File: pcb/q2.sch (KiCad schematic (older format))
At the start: 238 parts, among them U1 R, U10 R, U100 R, U101 R, U102 R, U103 R, U104 R, U105 R, U106 R, U107 R, U108 R, U109 R, U11 R, U110 R, U111 R, U112 R, U113 16, U114 R, U115 WiPy, U116 UDN_2981, U117 UDN_2981, U118 74HC595, U119 74HC595, U12 R, U13 R, U14 R, U15 R, U16 R, U17 R, U18 R, U19 R, U2 R, U20 R, U21 R, U22 R, U23 R, U24 R, U25 R, U26 R, U27 R, U28 R, U29 R, U3 R, U30 R, U31 R, U32 R, U33 R, U34 R, U35 R, U36 R, U37 R, U38 R, U39 R, U4 R, U40 R, U41 R, U42 R, U43 R, U44 R, U45 R, U46 R, U47 R, U48 R, U49 R, U5 R, U50 R, U51 R, U52 R, U53 R, U54 R, U55 R, U56 R, U57 R, U58 R, U59 R, U6 R, U60 R, U61 R, U62 R, U63 R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

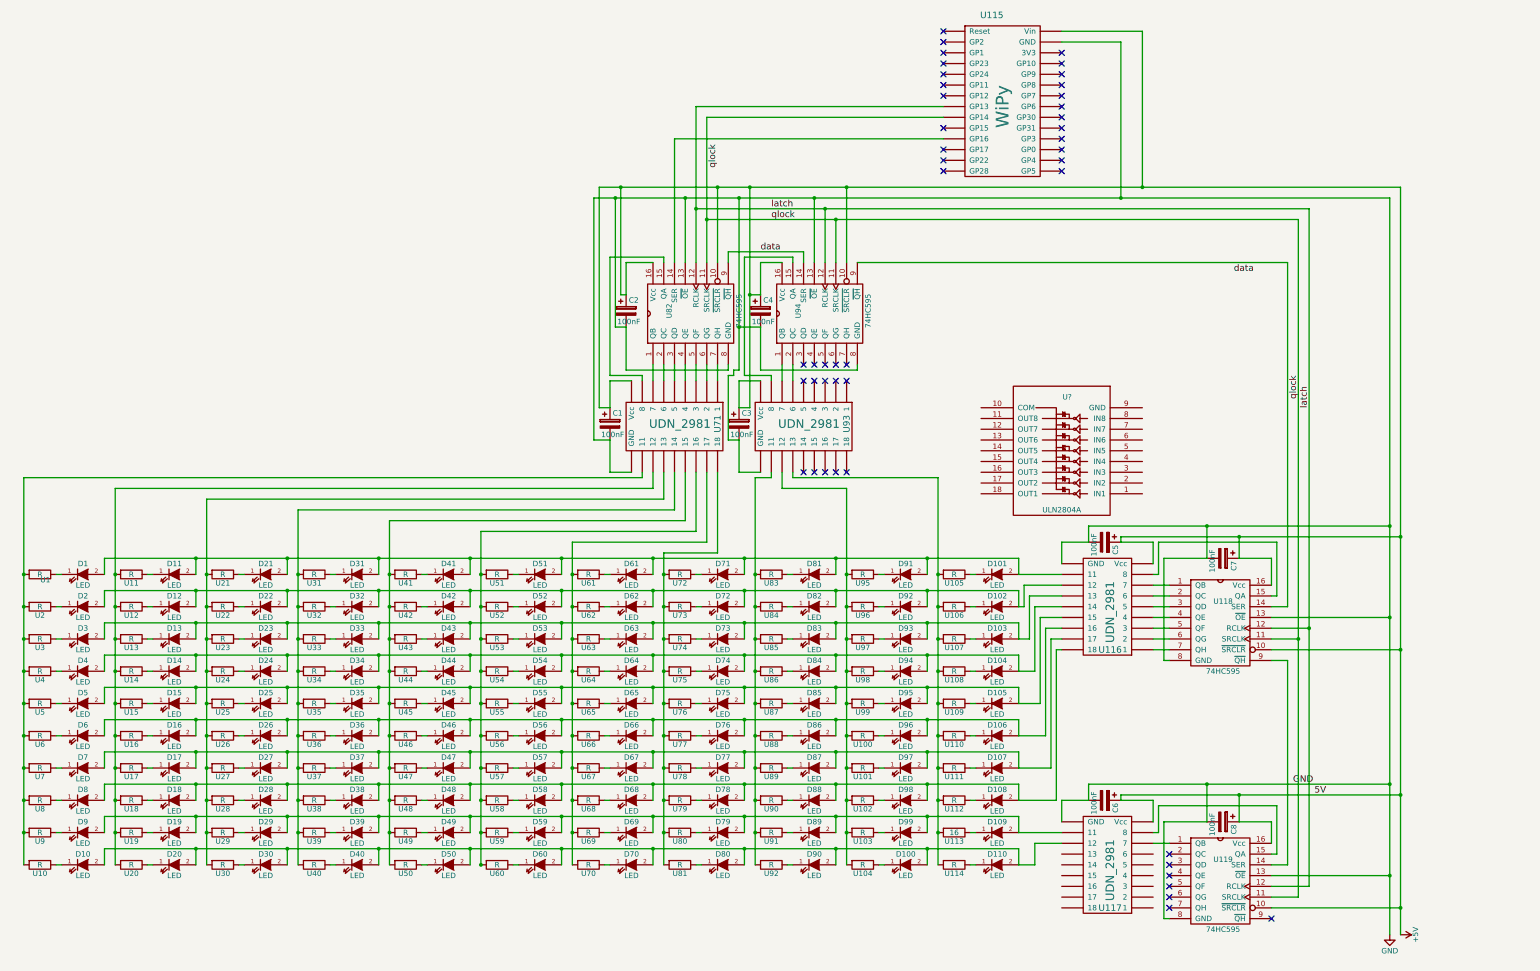
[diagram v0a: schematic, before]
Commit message: move cathode driver + SR to left side
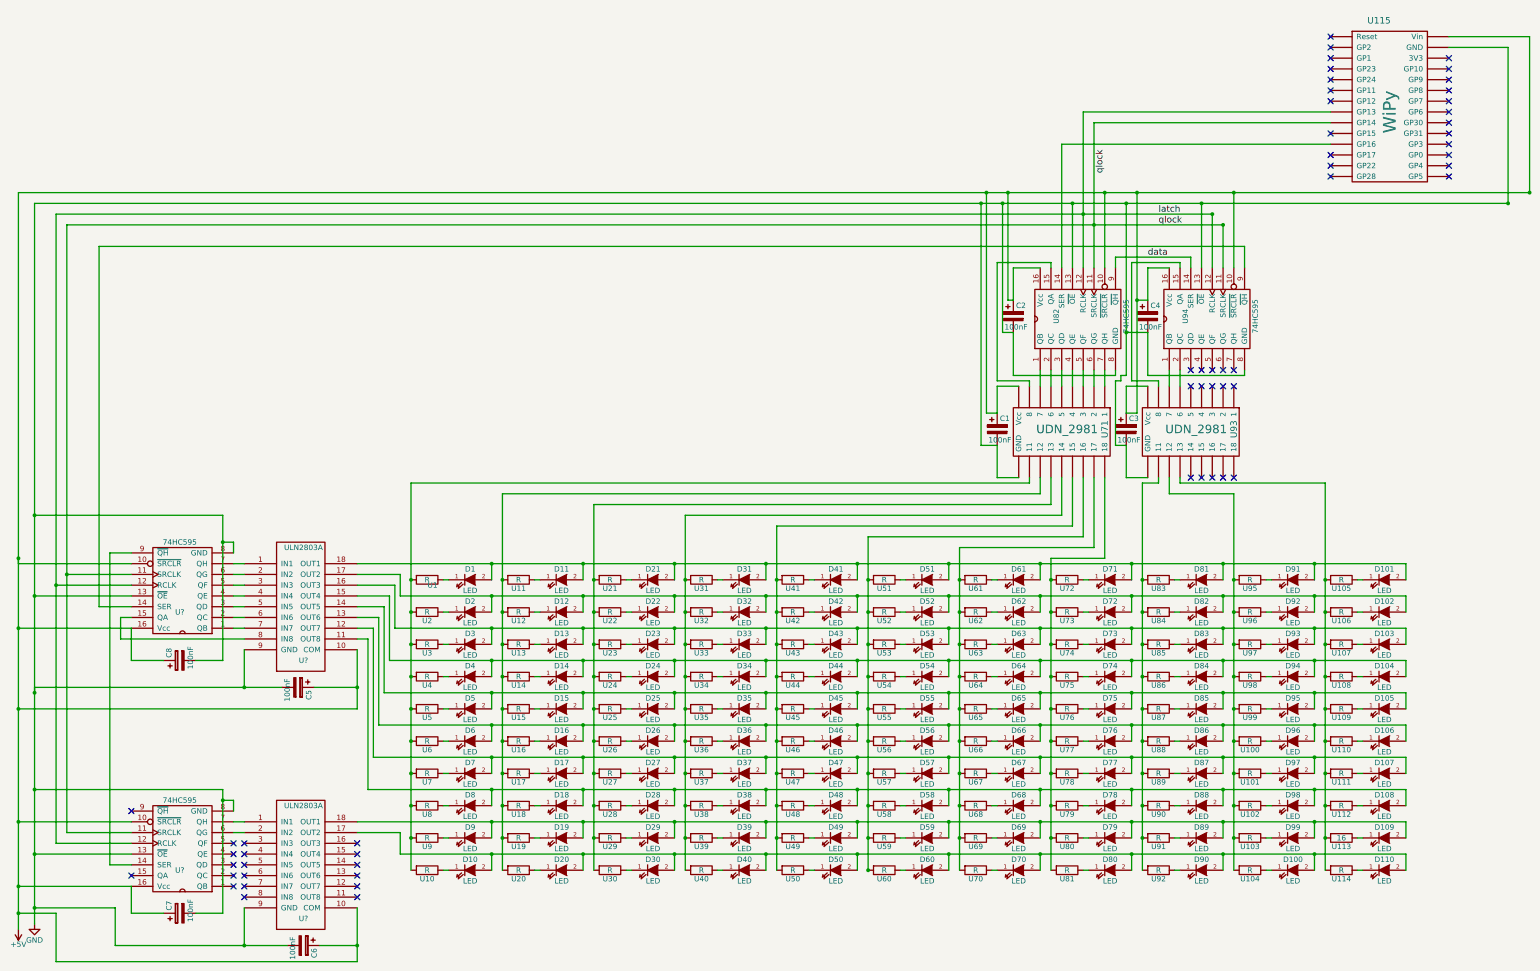
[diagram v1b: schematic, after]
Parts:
- removed U116, U117: UDN_2981, symbol UDN_2981
- removed U118, U119: 74HC595, symbol 74HC595
- removed U?: ULN2804A, symbol ULN2804A
- added U? (x2): ULN2803A, symbol ULN2803A
- added U? (x2): 74HC595, symbol 74HC595
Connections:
- net +5V: now also U?.10 (COM), U?.10 (COM), U?.10 (~SRCLR), U?.10 (~SRCLR), U?.16 (Vcc), U?.16 (Vcc)
- net GND: now also U?.13 (~OE), U?.13 (~OE), U?.8 (GND), U?.8 (GND), U?.9 (GND), U?.9 (GND)
- net latch: now also U?.12 (RCLK), U?.12 (RCLK)
- net qlock: now also U?.11 (SRCLK), U?.11 (SRCLK)
- net at D1.2 (A), D101.2 (A), D11.2 (A)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: now also U?.18 (OUT1)
- net at D102.2 (A), D12.2 (A), D2.2 (A)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: now also U?.17 (OUT2)
- net at D103.2 (A), D13.2 (A), D23.2 (A)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: now also U?.16 (OUT3)
- net at D104.2 (A), D14.2 (A), D24.2 (A)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: now also U?.15 (OUT4)
- net at D105.2 (A), D15.2 (A), D25.2 (A)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: now also U?.14 (OUT5)
- net at D106.2 (A), D16.2 (A), D26.2 (A)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: now also U?.13 (OUT6)
- net at D107.2 (A), D17.2 (A), D27.2 (A)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: now also U?.12 (OUT7)
- net at D108.2 (A), D18.2 (A), D28.2 (A)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: now also U?.11 (OUT8)
- net at D109.2 (A), D19.2 (A), D29.2 (A)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: now also U?.18 (OUT1)
- net at D10.2 (A), D100.2 (A), D110.2 (A)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: now also U?.17 (OUT2)
- net at U94.9 (~QH): now also U?.14 (SER)
- new net: U?.1 (IN1), U?.7 (QH) (x2)
- new net: U?.2 (IN2), U?.6 (QG) (x2)
- new net: U?.3 (IN3), U?.5 (QF)
- new net: U?.4 (IN4), U?.4 (QE)
- new net: U?.3 (QD), U?.5 (IN5)
- new net: U?.2 (QC), U?.6 (IN6)
- new net: U?.1 (QB), U?.7 (IN7)
- new net: U?.15 (QA), U?.8 (IN8)
- new net: U?.14 (SER), U?.9 (~QH)
- no-connect marks 45 -> 57
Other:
- moved on the sheet: C1, C2, C3, C4, C5, C6, C7, C8, D1, D10, D100, D101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

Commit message: capacitor for -OE to disable row shift register at startup
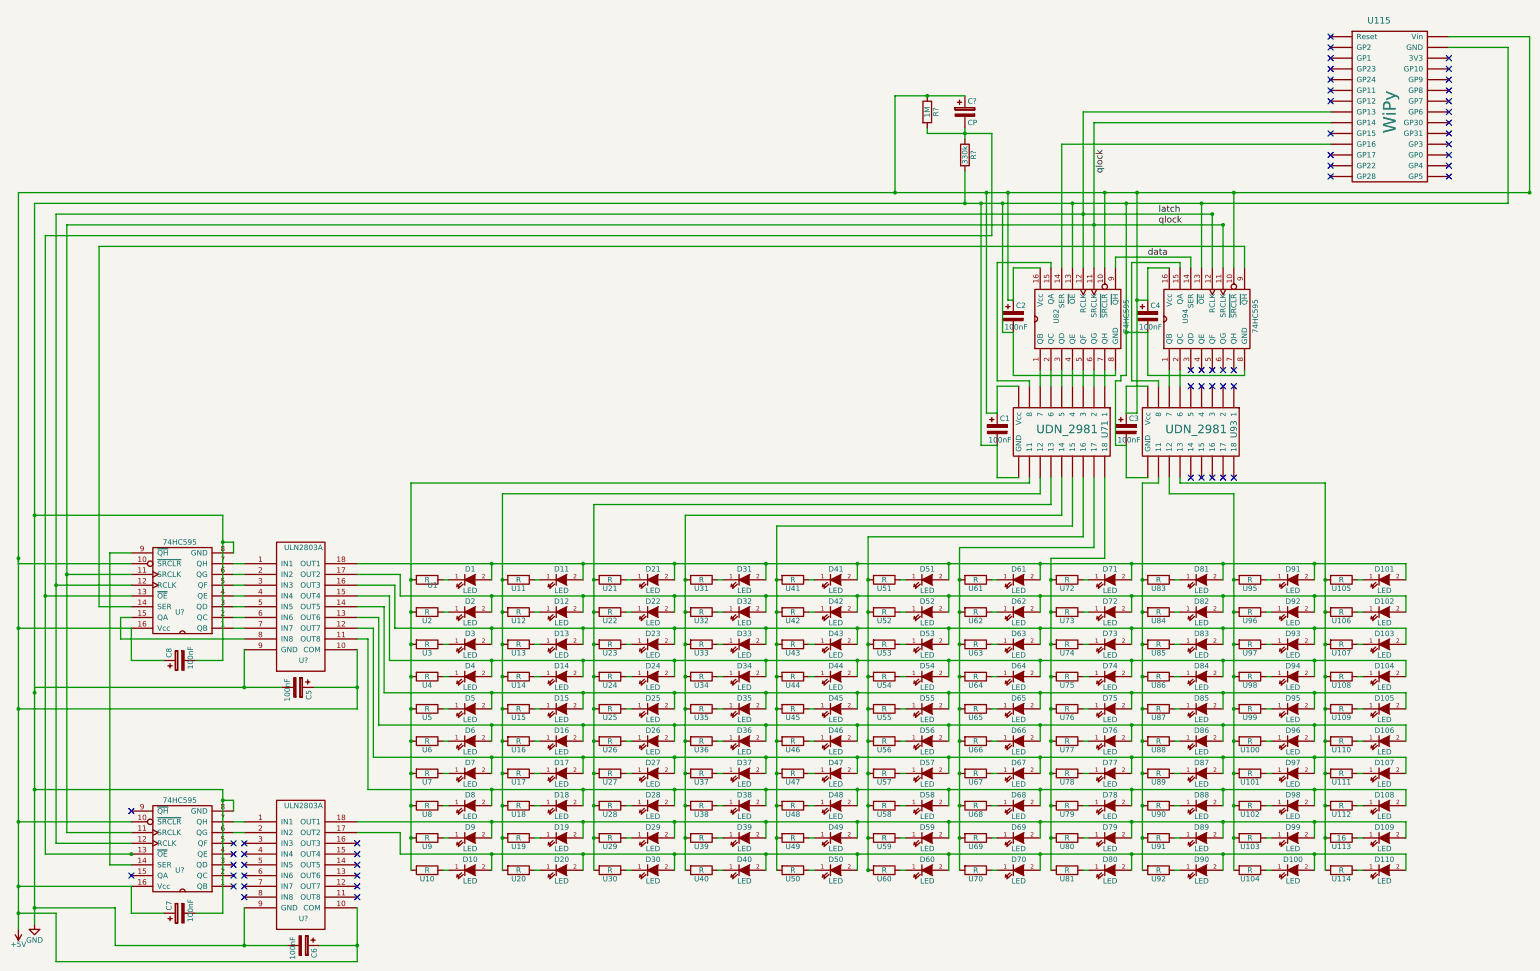
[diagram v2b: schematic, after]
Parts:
- added C?: CP, symbol CP
- added R?: 1M, symbol R
- added R?: 330k, symbol R
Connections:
- net +5V: now also C?.1, R?.1
- net GND: now also R?.2; no longer U?.13 (~OE), U?.13 (~OE)
- new net: C?.2, R?.1, R?.2, U?.13 (~OE), U?.13 (~OE)
